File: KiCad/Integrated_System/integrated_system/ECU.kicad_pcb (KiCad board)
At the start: 2 copper layers, 61.3 x 72.8 mm, 48 parts, among them J1 Jack-DC, J2 Fan 1, J3 Fan 2, J4 Fan 3, Q1 BSS138, Q2 BSS138, Q3 BSS138, SW1 SW_SPDT, SW2 SW_SPDT, SW3 SW_Push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

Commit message: made changes
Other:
- board text removed: "Add lots of vias"
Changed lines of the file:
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@@
 		(layer "Edge.Cuts")
-	)
-	(gr_text "Add lots of vias"
-		(at 198 88.25 0)
-		(layer "F.SilkS")
-		(effects
-			(font
-				(size 1.5 1.5)
-				(thickness 0.3)
-				(bold yes)
-			)
-			(justify left bottom)
-		)
 	)
 	(gr_text "4/23/2026"
@@
 		)
 	)
+	(gr_text_box "Notes\n\n- Add more vias"
+		(start 189.75 79.5)
+		(end 223 117.25)
+		(margins 1.0025 1.0025 1.0025 1.0025)
+		(layer "Cmts.User")
+		(effects
+			(font
+				(size 1 1)
+				(thickness 0.15)
+			)
+			(justify left top)
+		)
+		(border yes)
+		(stroke
+			(width 0.1)
+			(type solid)
+		)
+	)

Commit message: deleted all traces
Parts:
- added R15: 4.7k, Resistor_SMD:R_1206_3216Metric_Pad1.30x1.75mm_HandSolder, F.Cu at (98.0, 124.4)
- added R16: 4.7k, Resistor_SMD:R_1206_3216Metric_Pad1.30x1.75mm_HandSolder, F.Cu at (98.0, 127.8)
- R12, R13, R14: value 330 -> 1k
- turned C1 to -90 degrees
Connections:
- C3 pad 1: VDD -> VDD (+ 3.3 V)
- C4 pad 1: VDD -> VDD (+ 3.3 V)
- C5 pad 1: VDD -> VDD (+ 3.3 V)
- D10 pad 1: Net-(D10-K) -> GND
- D10 pad 2: Net-(A1-A10/IO27) -> Net-(D10-A)
- D11 pad 1: Net-(D11-K) -> GND
- D11 pad 2: Net-(A1-A11/IO12) -> Net-(D11-A)
- D9 pad 1: Net-(D9-K) -> GND
- D9 pad 2: Net-(A1-A9/IO33) -> Net-(D9-A)
- R12 pad 1: GND -> Net-(D9-A)
- R12 pad 2: Net-(D9-K) -> Net-(A1-A9/IO33)
- R13 pad 1: GND -> Net-(D10-A)
- R13 pad 2: Net-(D10-K) -> Net-(A1-A10/IO27)
- R14 pad 1: GND -> Net-(D11-A)
- R14 pad 2: Net-(D11-K) -> Net-(A1-A11/IO12)
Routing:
- net FP_12V: track 186.9 -> 0.00 mm
- net +12V AC to DC wall adapter: track 62.4 -> 0.00 mm
- net Net-(A1-I34/A2): track 39.7 -> 0.00 mm
- net Net-(A1-DAC1/A1): track 31.4 -> 0.00 mm
- net Net-(A1-DAC2/A0): track 26.5 -> 0.00 mm, vias 0 -> 1
- net Net-(D4-K): track 25.0 -> 0.00 mm
- net Net-(D5-K): track 24.1 -> 0.00 mm
- net Net-(D8-A): track 24.0 -> 0.00 mm
- net Net-(D7-A): track 23.4 -> 0.00 mm
- net Net-(A1-IO4/A5): track 22.7 -> 0.00 mm
- net Net-(D6-A): track 21.4 -> 0.00 mm
- net Net-(Q3-G): track 20.2 -> 0.00 mm
- net Net-(Q2-G): track 19.7 -> 0.00 mm
- net Net-(Q1-G): track 19.7 -> 0.00 mm
- net VDD (+ 3.3 V): track 8.50 -> 0.00 mm
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
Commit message: redesign
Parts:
- removed RV1: Pot1_Control, Potentiometer_THT:Potentiometer_Bourns_3296W_Vertical
- moved R12 52.8 mm to (140.0, 122.5), turned to 90 degrees
- moved R16 52.2 mm to (147.8, 112.0), turned to 180 degrees
- moved R15 50.6 mm to (147.8, 115.8), turned to 180 degrees
- moved C6 46.9 mm to (146.8, 123.5)
- moved R13 46.8 mm to (132.0, 122.5), turned to 90 degrees
- moved R14 42.9 mm to (136.0, 122.5), turned to 90 degrees
- moved U4 36.1 mm to (150.8, 109.9)
- moved C4 34.2 mm to (113.0, 70.0)
- moved D11 32.2 mm to (109.0, 85.2)
- moved SW3 28.5 mm to (112.2, 103.5), turned to 90 degrees
- moved D10 26.4 mm to (109.0, 80.0), turned to -90 degrees
- moved D9 21.1 mm to (109.0, 74.8)
- moved SW4 21.0 mm to (112.2, 93.8), turned to 90 degrees
- moved R5 19.8 mm to (128.0, 122.5)
- moved C2 16.2 mm to (149.2, 73.0), turned to 0 degrees
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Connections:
- D11 pad 1: GND -> (no net)
- D11 pad 2: Net-(D11-A) -> (no net)
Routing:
- net Net-(Q3-G): vias 2 -> 0
- net Net-(Q2-G): vias 2 -> 0
- net Net-(Q1-G): vias 2 -> 0
- net Net-(D8-A): vias 1 -> 0
- net Net-(D7-A): vias 1 -> 0
- net Net-(D6-A): vias 1 -> 0
- net Net-(D5-K): vias 1 -> 0
- net Net-(D4-K): vias 1 -> 0
- net Net-(D3-K): vias 1 -> 0
- net Net-(D2-K): vias 1 -> 0
- net Net-(A1-IO4/A5): vias 1 -> 0
- net Net-(A1-IO36/A4): vias 0 -> 1
- net Net-(A1-I34/A2): vias 2 -> 0
- net Net-(A1-DAC2/A0): vias 1 -> 0
- net Net-(A1-DAC1/A1): vias 2 -> 0
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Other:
- board text added: "OSSEM v1.4"
- board text removed: "OSSEM v1.3"

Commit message: small adjustments
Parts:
- added C7: 0.1u, Capacitor_SMD:C_1206_3216Metric_Pad1.33x1.80mm_HandSolder, F.Cu at (134.2, 136.2)
- added J5: Conn_01x04, Connector_PinSocket_2.54mm:PinSocket_1x04_P2.54mm_Vertical, F.Cu at (122.0, 136.0)
- added R17: 0, Resistor_SMD:R_1206_3216Metric_Pad1.30x1.75mm_HandSolder, F.Cu at (124.0, 122.0)
- added TP1: TestPoint, Connector_Pin:Pin_D0.7mm_L6.5mm_W1.8mm_FlatFork, F.Cu at (112.8, 120.8)
- added TP2: TestPoint, Connector_Pin:Pin_D0.7mm_L6.5mm_W1.8mm_FlatFork, F.Cu at (165.0, 108.0)
- added TP3: TestPoint, Connector_Pin:Pin_D0.7mm_L6.5mm_W1.8mm_FlatFork, F.Cu at (151.8, 125.0)
- added TP4: TestPoint, Connector_Pin:Pin_D0.7mm_L6.5mm_W1.8mm_FlatFork, F.Cu at (128.5, 121.8)
- added TP5: TestPoint, Connector_Pin:Pin_D0.7mm_L6.5mm_W1.8mm_FlatFork, F.Cu at (140.5, 121.8)
- moved C2 36.5 mm to (159.8, 108.0)
- moved R16 18.7 mm to (132.0, 122.0), turned to -90 degrees
- moved R15 13.5 mm to (135.8, 122.0), turned to -90 degrees
- moved R12 6.75 mm to (140.0, 129.2)
- moved R13 6.75 mm to (132.0, 129.2)
- moved R14 6.75 mm to (136.0, 129.2)
- moved R4 6.75 mm to (124.0, 129.2)
- moved R5 6.75 mm to (128.0, 129.2)
- moved C6 6.25 mm to (146.8, 129.8)
- moved U4 2.85 mm to (148.1, 110.6)
- moved C1 1.12 mm to (116.5, 127.8), turned to -90 degrees
- moved D4 0.75 mm to (110.0, 109.0)
- moved D5 0.75 mm to (110.0, 115.8)
- moved J1 0.25 mm to (155.4, 129.9)
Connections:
- A1 pad 8: Net-(A1-I39/A3) -> unconnected-(A1-I39/A3-Pad8)
- C6 pad 1: VDD (+ 3.3 V) -> Net-(U4-Vout+)
- D1 pad 2: FP_12V -> Net-(D1-A)
- D11 pad 1: (no net) -> GND
- D11 pad 2: (no net) -> Net-(D11-A)
- D2 pad 2: FP_12V -> Net-(D2-A)
- D6 pad 2: Net-(D6-A) -> Net-(D1-K)
- D7 pad 2: Net-(D7-A) -> Net-(D2-K)
- J2 pad 1: Net-(D6-A) -> Net-(D1-K)
- J3 pad 1: Net-(D7-A) -> Net-(D2-K)
- Q1 pad 3: Net-(D6-A) -> Net-(D1-K)
- Q2 pad 3: Net-(D7-A) -> Net-(D2-K)
- R1 pad 1: Net-(D1-K) -> FP_12V
- R1 pad 2: Net-(D6-A) -> Net-(D1-A)
- R2 pad 1: Net-(D2-K) -> FP_12V
- R2 pad 2: Net-(D7-A) -> Net-(D2-A)
- U4 pad 3: VDD (+ 3.3 V) -> Net-(U4-Vout+)
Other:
- board text added: "3V3"
- board text added: "GND"
- board text added: "SCD30"
- board text added: "SCL"
- board text added: "SDA"

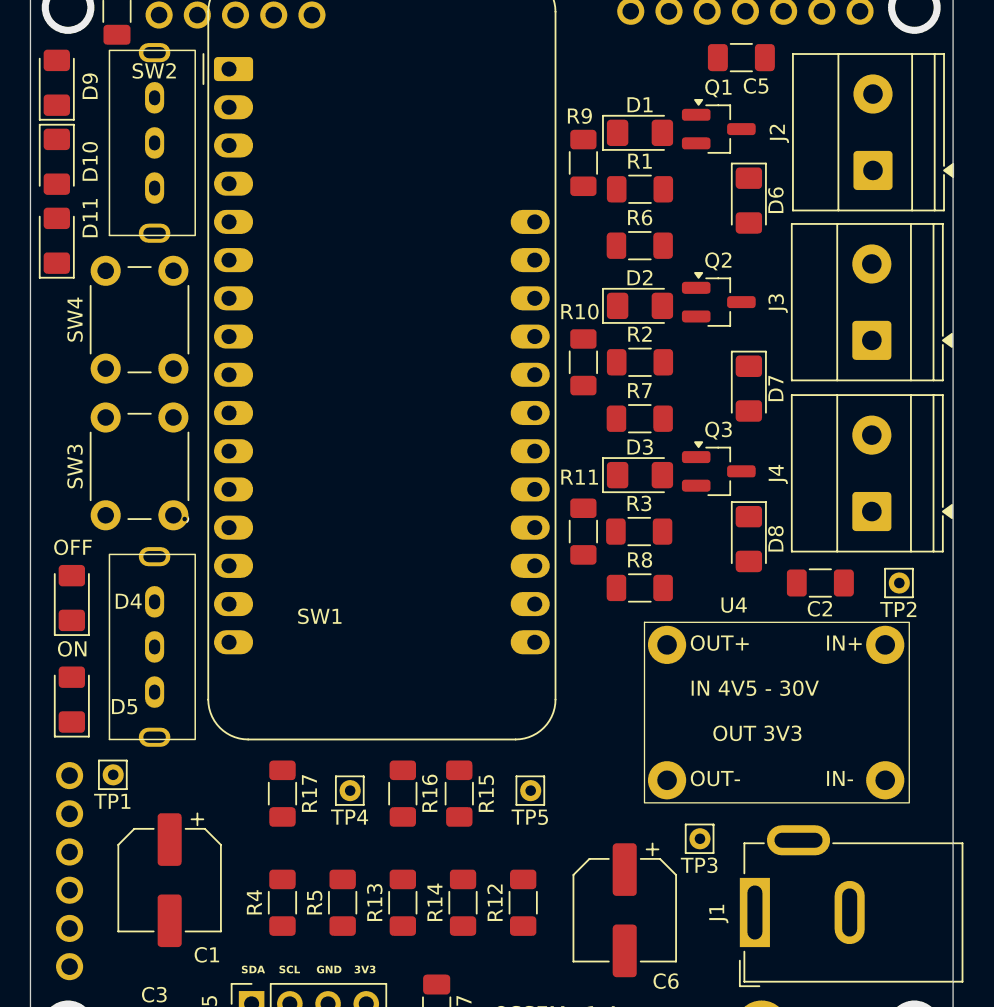
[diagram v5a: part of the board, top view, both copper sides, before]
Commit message: initial routing started
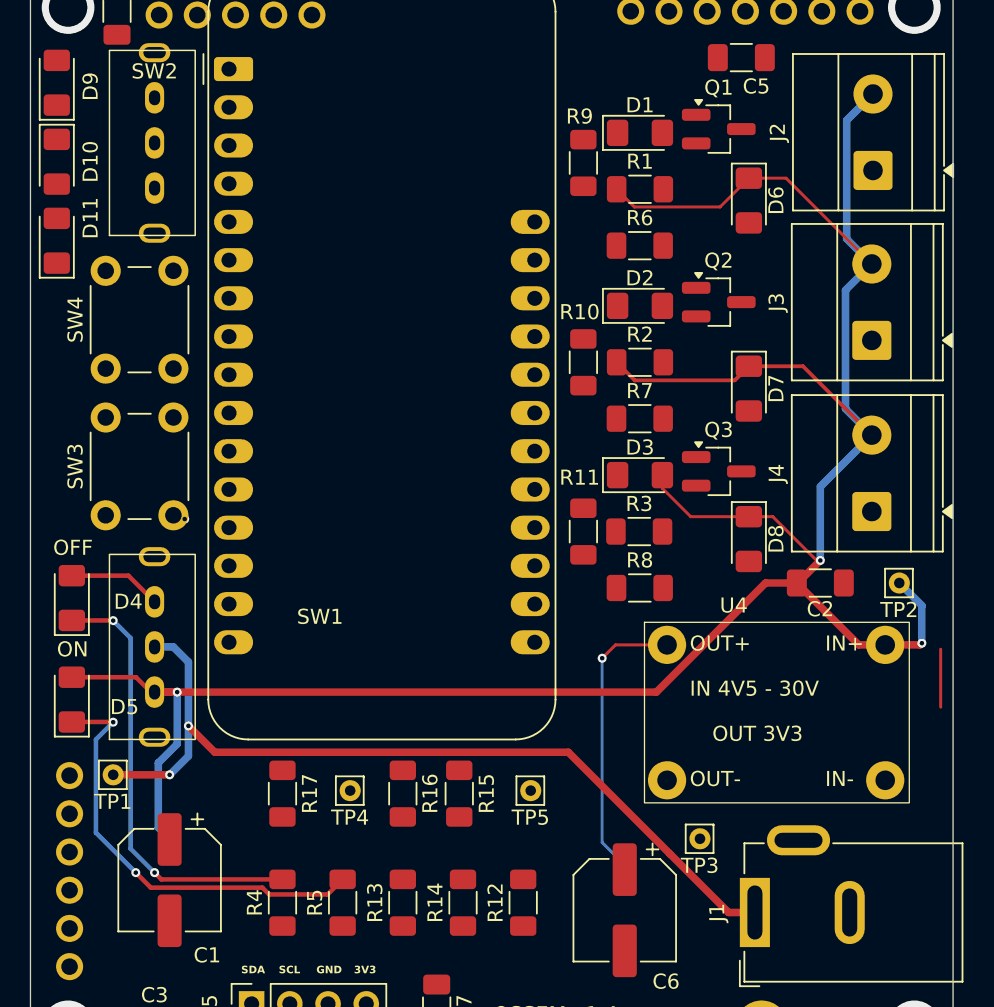
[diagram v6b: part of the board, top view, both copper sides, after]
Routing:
- net FP_12V: track 0.00 -> 169.5 mm, vias 0 -> 3
- net +12V AC to DC wall adapter: track 0.00 -> 57.2 mm, vias 0 -> 2
- net Net-(D4-K): track 0.00 -> 29.3 mm, vias 0 -> 2
- net Net-(D5-K): track 0.00 -> 29.1 mm, vias 0 -> 2
- net Net-(U4-Vout+): track 0.00 -> 22.9 mm, vias 0 -> 1
- net Net-(D4-A): track 0.00 -> 6.22 mm

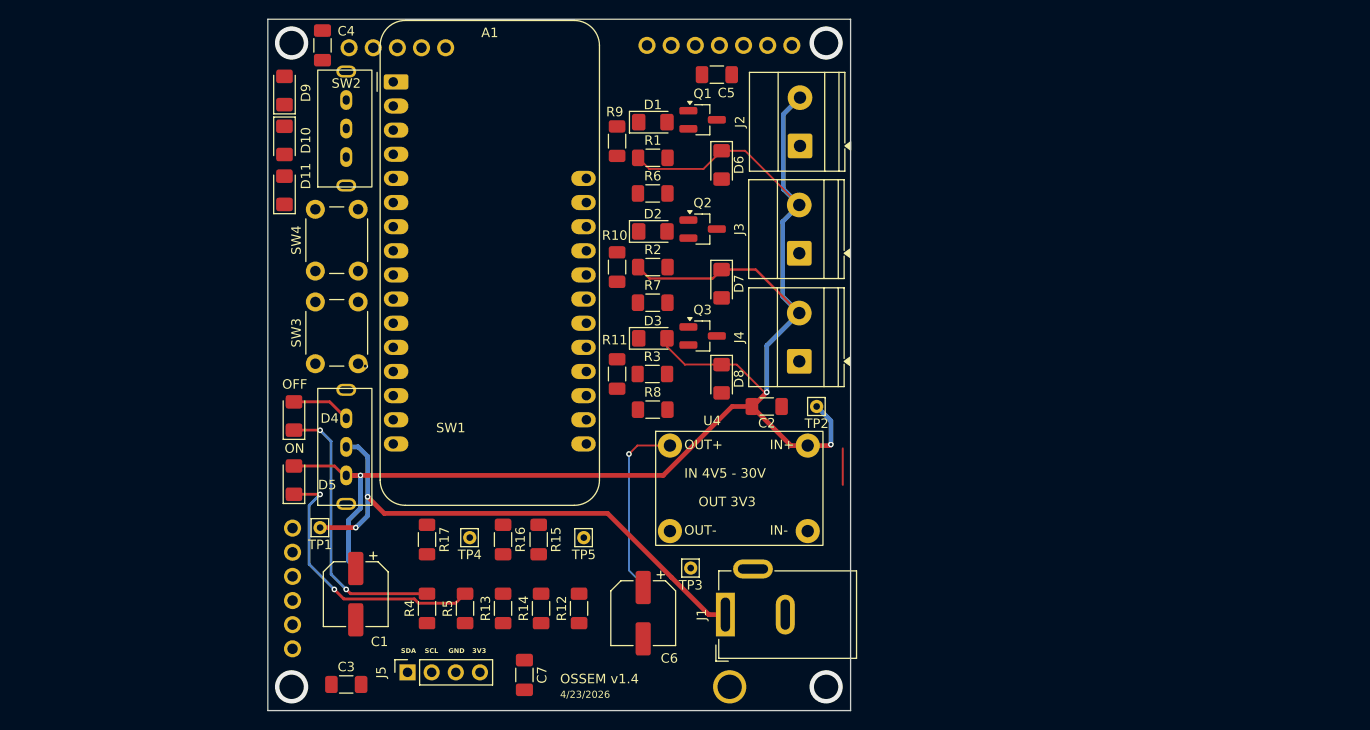
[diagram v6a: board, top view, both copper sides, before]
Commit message: Routing Complete
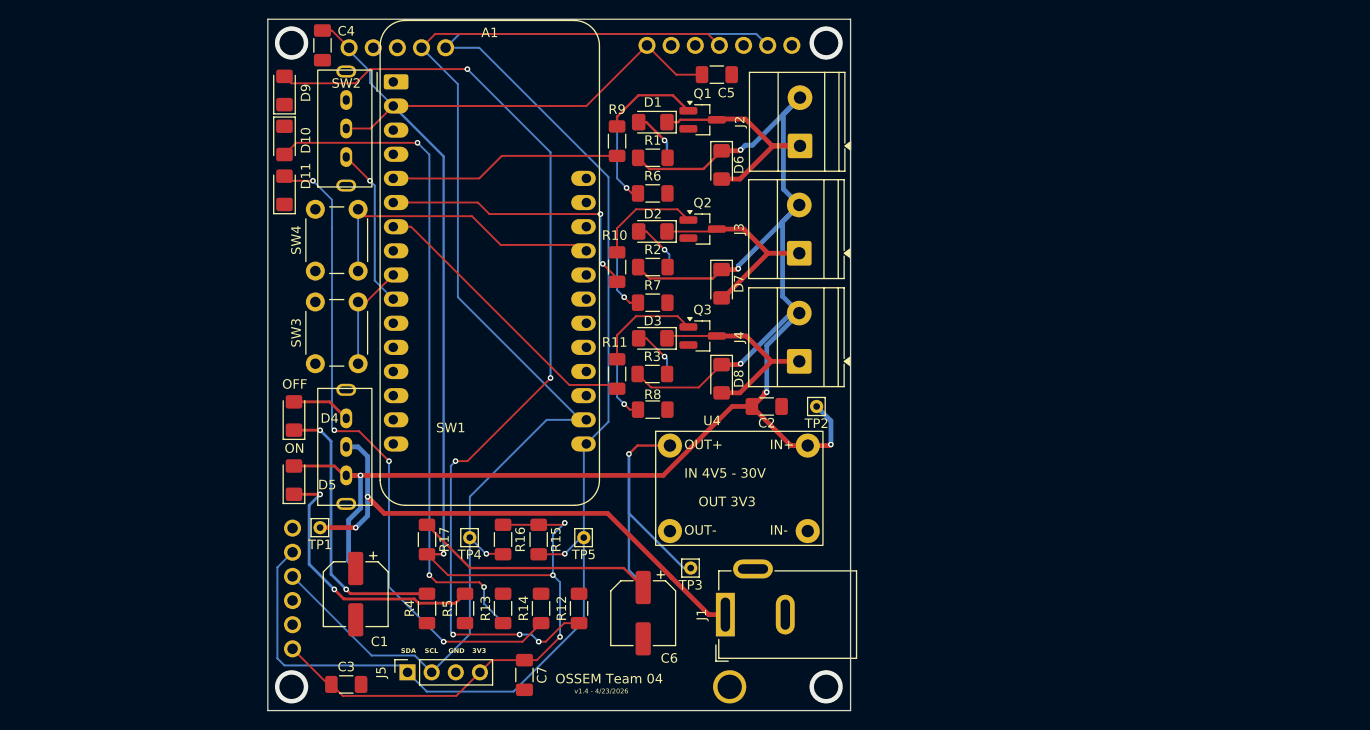
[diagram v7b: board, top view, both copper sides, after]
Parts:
- turned D1 to 180 degrees
- turned D2 to 180 degrees
- turned D3 to 180 degrees
- turned R10 to -90 degrees
- turned R11 to -90 degrees
- turned R6 to 180 degrees
- turned R7 to 180 degrees
- turned R8 to 180 degrees
- turned R9 to -90 degrees
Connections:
- D3 pad 2: FP_12V -> Net-(D3-A)
- D8 pad 2: Net-(D8-A) -> Net-(D3-K)
- J4 pad 1: Net-(D8-A) -> Net-(D3-K)
- Q3 pad 3: Net-(D8-A) -> Net-(D3-K)
- R3 pad 1: Net-(D3-K) -> FP_12V
- R3 pad 2: Net-(D8-A) -> Net-(D3-A)
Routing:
- net VDD (+ 3.3 V): track 0.00 -> 171.4 mm, vias 0 -> 4
- net Net-(A1-SDA/IO23): track 0.00 -> 159.7 mm, vias 0 -> 1
- net Net-(A1-SCL/IO22): track 0.00 -> 138.0 mm, vias 0 -> 1
- net Net-(D9-A): track 0.00 -> 102.9 mm, vias 0 -> 6
- net Net-(D10-A): track 0.00 -> 71.4 mm, vias 0 -> 3
- net Net-(D11-A): track 0.00 -> 69.9 mm, vias 0 -> 4
- net Net-(U4-Vout+): track 22.9 -> 59.7 mm
- net Net-(A1-A12/IO13): track 0.00 -> 32.3 mm
- net Net-(A1-I34/A2): track 0.00 -> 30.6 mm
- net Net-(A1-DAC1/A1): track 0.00 -> 30.2 mm, vias 0 -> 2
- net Net-(D1-K): track 0.00 -> 25.0 mm
- net Net-(A1-DAC2/A0): track 0.00 -> 24.5 mm
- net Net-(D2-K): track 0.00 -> 21.9 mm
- net Net-(D3-K): track 0.00 -> 21.8 mm
- net Net-(Q1-G): track 0.00 -> 18.5 mm, vias 0 -> 1
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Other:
- board text added: "MOX Gas Sensor"
- board text added: "OSSEM Team 04"
- board text added: "v1.4 - 4/23/2026"
- board text removed: "4/23/2026"
- board text removed: "OSSEM v1.4"

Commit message: added copper ground layers
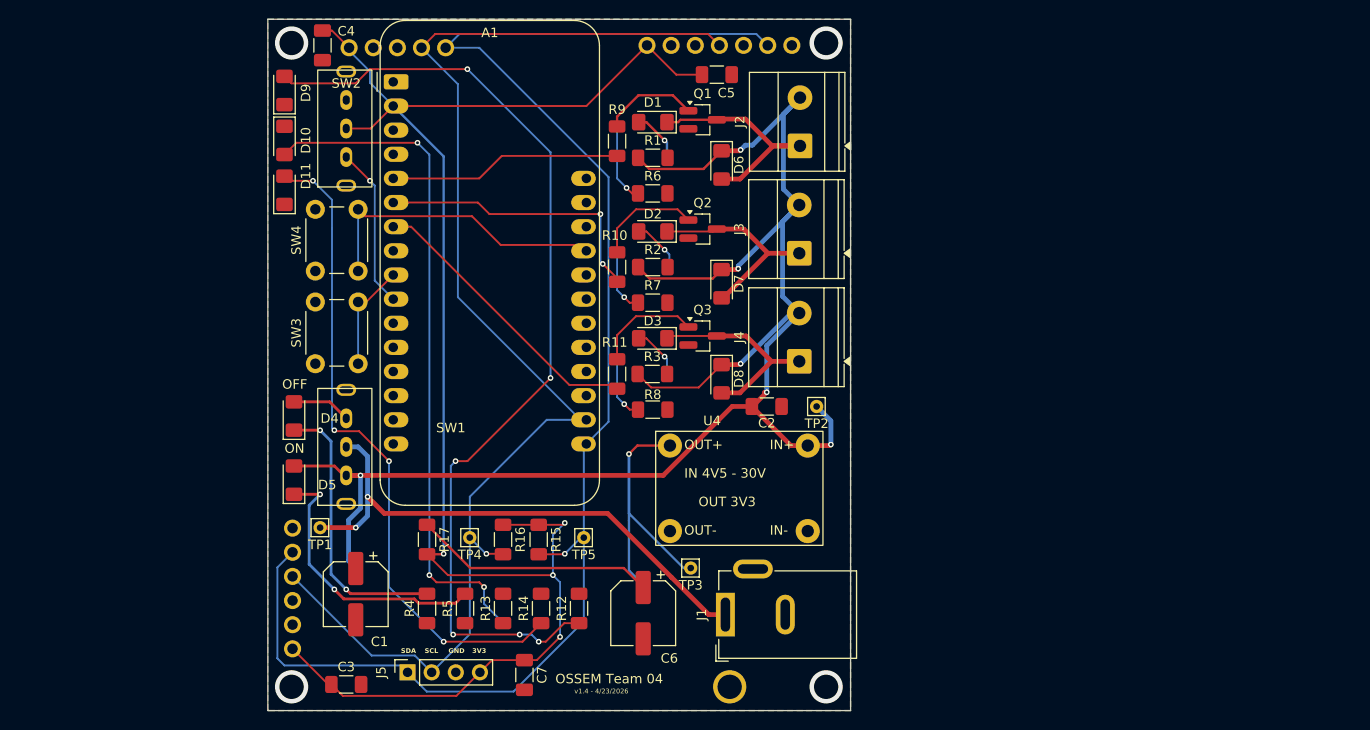
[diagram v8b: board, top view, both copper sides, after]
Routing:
- added copper zone on B.Cu, net GND
- added copper zone on F.Cu, net GND
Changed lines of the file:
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@@
 	)
 	(gr_text_box "Notes\n\n- Add more vias"
-		(start 189.75 79.5)
-		(end 223 117.25)
+		(start 180.875 84.75)
+		(end 214.125 122.5)
 		(margins 1.0025 1.0025 1.0025 1.0025)
 		(layer "Cmts.User")
@@
 		(net 53)
 	)
+	(zone
+		(net 18)
+		(net_name "GND")
+		(layers "F.Cu" "B.Cu")
+		(hatch edge 0.5)
+		(connect_pads
+			(clearance 0.5)
+		)
+		(min_thickness 0.25)
+		(filled_areas_thickness no)
+		(fill yes
+			(thermal_gap 0.5)
+			(thermal_bridge_width 0.5)
+		)
+		(polygon
+			(pts
+				(xy 107.25 67.25) (xy 168.5725 67.25) (xy 168.5725 140) (xy 107.25 140)
+			)
+		)
+	)
 	(embedded_fonts no)
